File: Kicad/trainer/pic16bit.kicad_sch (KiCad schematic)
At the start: 30 parts, among them K101 AC/DC 9-12V, K102 AC/DC 9-12V, K103 PE-450-4X6X-BLACK, U101 KEYSTONE-24283, U102 KEYSTONE-24283, U103 KEYSTONE-24283, U104 KEYSTONE-24283, U105 NCP5662-ADJ, X101 3M-SJ5376, X102 3M-SJ5376, X103 3M-SJ5376, X104 3M-SJ5376, X105 3M-SJ5376

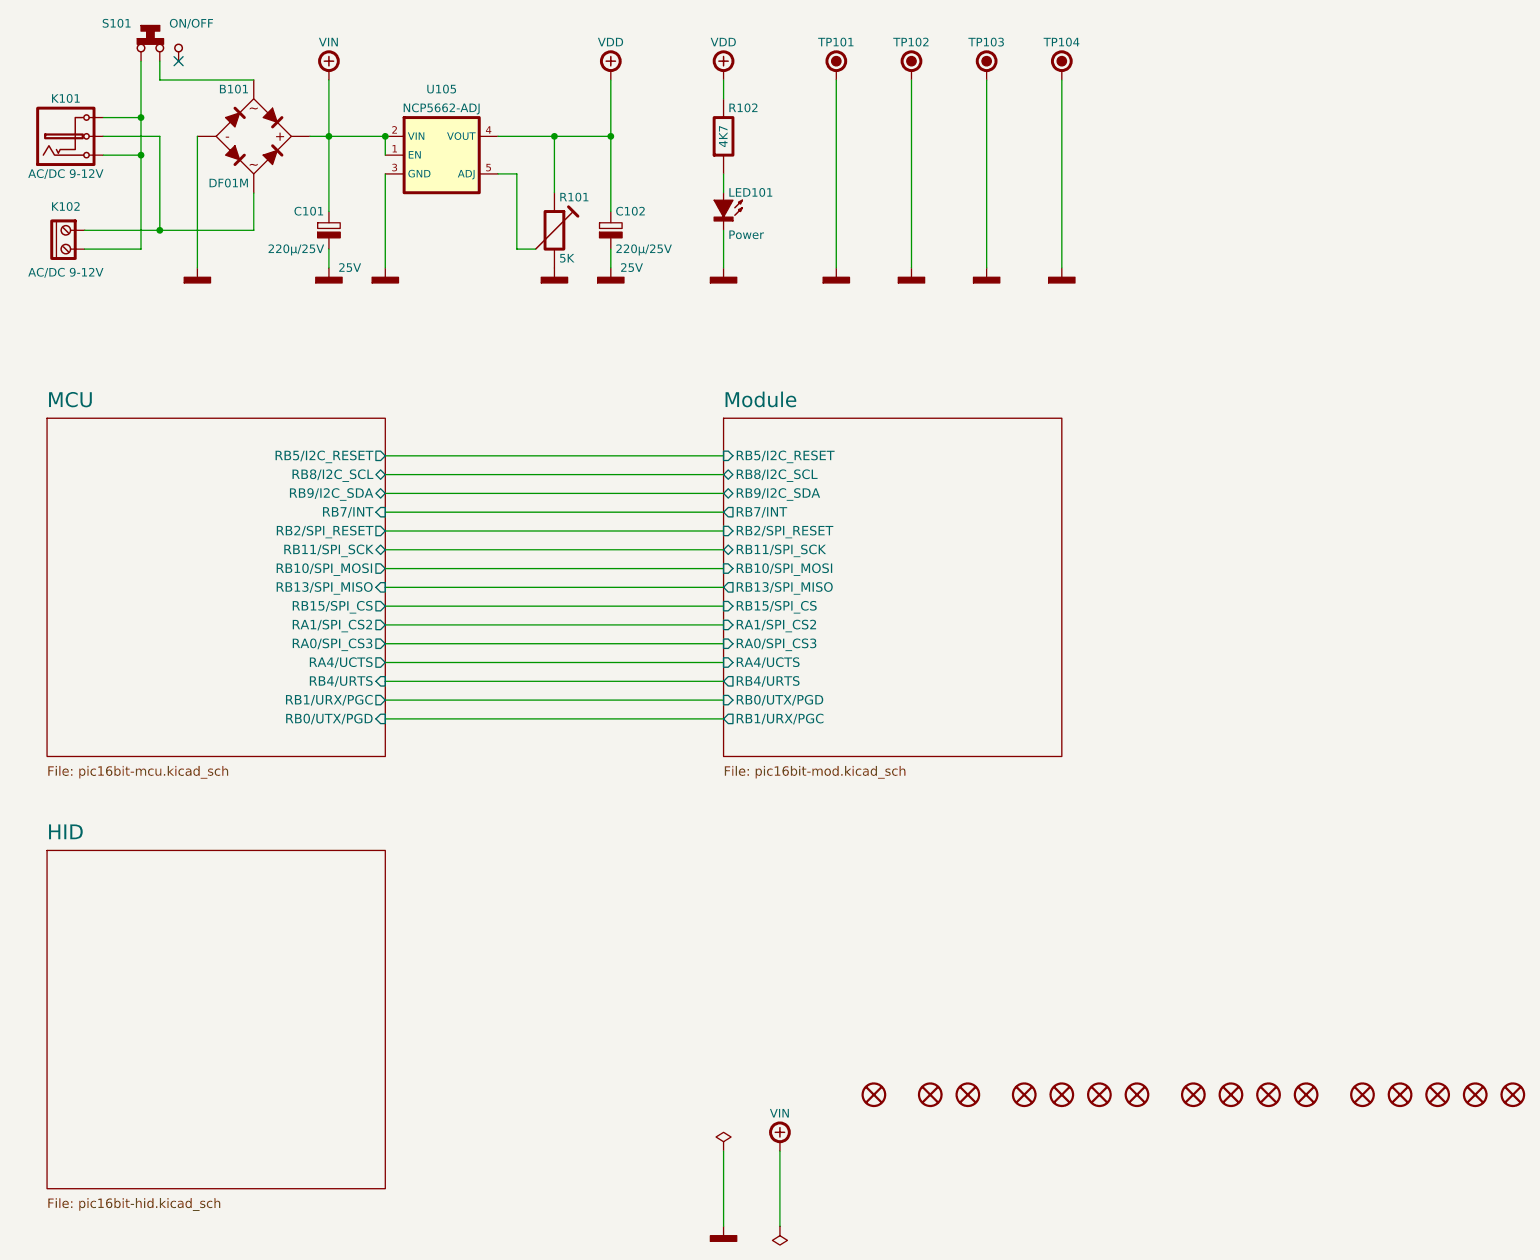
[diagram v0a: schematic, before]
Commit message: Update Trainer Kicad 8
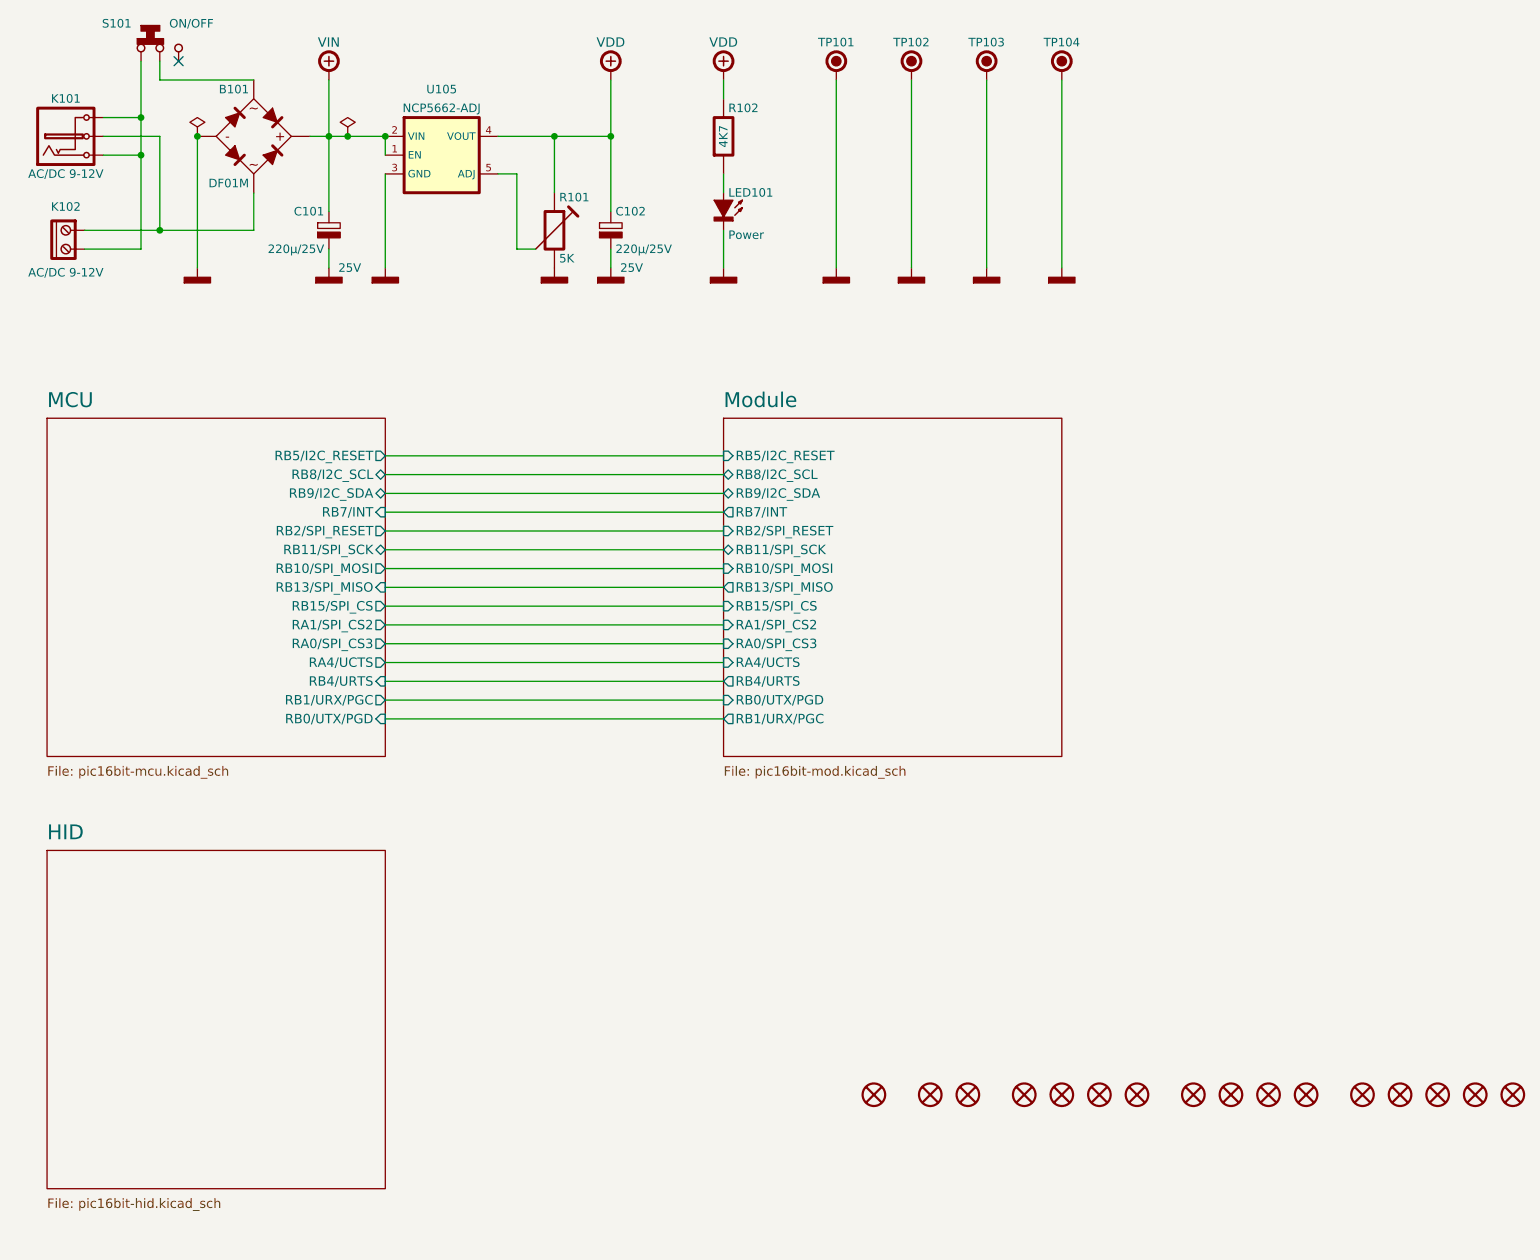
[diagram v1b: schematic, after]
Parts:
- LED101: footprint tronixio:LED-TH-05MM -> tronixio:LED-TH-ROUND-05MM; symbol tronixio:KINGBRIGHT-LED-05MM-TH -> tronixio:KINGBRIGHT-LED-05MM-RED
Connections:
- net +VDD renamed POWER-VDD
- net +VIN renamed POWER-VIN
- net GND renamed POWER-GND

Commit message: Up
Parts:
- U105: footprint tronixio:TO-263-5 -> tronixio:TO-263-5-TABPIN3
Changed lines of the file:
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@@
 			)
 		)
-		(property "Footprint" "tronixio:TO-263-5"
+		(property "Footprint" "tronixio:TO-263-5-TABPIN3"
 			(at 129.54 55.88 0)
 			(effects

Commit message: Up
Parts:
- K101: footprint tronixio:CUI-PJ-102AH -> tronixio:SSD-PJ-102AH; symbol tronixio:CUI-PJ-102AH-TH -> tronixio:SSD-PJ-102AH-TH
- K102: footprint tronixio:CUI-TB006-508-02BE -> tronixio:SSD-TB006-508-02BE; symbol tronixio:CUI-TB006-508-02BE -> tronixio:SSD-TB006-508-02BE
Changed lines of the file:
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@@
 	)
 	(symbol
-		(lib_id "tronixio:CUI-TB006-508-02BE")
+		(lib_id "tronixio:SSD-TB006-508-02BE")
 		(at 78.74 55.88 0)
 		(mirror y)
@@
 			)
 		)
-		(property "Footprint" "tronixio:CUI-TB006-508-02BE"
+		(property "Footprint" "tronixio:SSD-TB006-508-02BE"
 			(at 78.74 66.04 0)
 			(effects
@@
 			)
 		)
-		(property "Datasheet" "https://www.cuidevices.com/product/interconnect/connectors/terminal-blocks/tb006-508-series"
+		(property "Datasheet" "https://www.sameskydevices.com/product/interconnect/connectors/terminal-blocks/tb006-508-series"
 			(at 78.74 68.58 0)
 			(effects
@@
 	)
 	(symbol
-		(lib_id "tronixio:CUI-PJ-102AH-TH")
+		(lib_id "tronixio:SSD-PJ-102AH-TH")
 		(at 78.74 43.18 0)
 		(unit 1)
@@
 			)
 		)
-		(property "Footprint" "tronixio:CUI-PJ-102AH"
+		(property "Footprint" "tronixio:SSD-PJ-102AH"
 			(at 78.74 50.8 0)
 			(effects
@@
 			)
 		)
-		(property "Datasheet" "https://www.cuidevices.com/product/interconnect/connectors/dc-power-connectors/jacks/pj-102ah"
+		(property "Datasheet" "https://www.sameskydevices.com/product/interconnect/connectors/dc-power-connectors/jacks/pj-102ah"
 			(at 78.74 53.34 0)
 			(effects

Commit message: Up
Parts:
- K101: footprint tronixio:SSD-PJ-102AH -> tronixio:SAMESKY-PJ-102AH; symbol tronixio:SSD-PJ-102AH-TH -> tronixio:SAMESKY-PJ-102AH-TH
- K102: footprint tronixio:SSD-TB006-508-02BE -> tronixio:SAMESKY-TB006-508-02BE; symbol tronixio:SSD-TB006-508-02BE -> tronixio:SAMESSKY-TB006-508-02BE
